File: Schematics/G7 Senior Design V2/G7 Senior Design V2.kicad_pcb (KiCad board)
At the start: 2 copper layers, 100 x 100 mm, 45 parts, among them IC3 UART, J1 USB, J2 JCK, J3 PPTC191LFBN-RC, J4 PPTC191LFBN-RC, Q1 T1, Q2 T2, U1 ESP32-WROOM-32-N4, U2 DWM1000, U3 AMS1117-3.3

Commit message: One Page Error Report Gerber
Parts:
- added G***: LOGO, SD V2 ESP32 Components:UCF Logo 2, F.Cu at (138.5, 102.5)
- added G***: LOGO, SD V2 ESP32 Components:CitronautHeadFootprint, B.Cu at (149.5, 61.0)
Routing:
- net /EN: track 108.0 -> 159.1 mm, vias 6 -> 10
- net Net-(U1-CLK): track 117.6 -> 84.6 mm
- net Net-(Q2-Pad1): track 0.00 -> 28.1 mm, vias 0 -> 2
- net Net-(IC3-DTR): track 7.75 -> 16.6 mm
- net Net-(U1-IO18): track 93.9 -> 89.9 mm
- net /IO0: track 129.1 -> 132.8 mm
- net Net-(IC3-TXD): track 95.2 -> 93.3 mm
- net Net-(U1-IO15): track 44.3 -> 43.1 mm
- net Net-(IC3-VBUS): track 72.4 -> 73.5 mm
- net Net-(U1-CMD): track 91.3 -> 90.4 mm
- net Net-(U1-IO34): track 109.8 -> 109.1 mm
- net GND: track 329.3 -> 328.6 mm
- net Net-(U1-IO2): track 44.0 -> 44.7 mm

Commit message: Updated Gerber and BOM 13 SEP 24
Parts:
- C19: footprint SD V2 USB to UART Components:CAPC2012X95N -> SD V2 USB to UART Components:CAPC2012X145N
- R31: value RD1 -> 1K; footprint SD V2 USB to UART Components:RES_1220_SUS -> SD V2 DW1000 Components:RC0805N_YAG
- R32: value RD2 -> 1K; footprint SD V2 USB to UART Components:RES_1220_SUS -> SD V2 DW1000 Components:RC0805N_YAG
- R33: value RD3 -> 1K; footprint SD V2 USB to UART Components:RES_1220_SUS -> SD V2 DW1000 Components:RC0805N_YAG
- moved R33 0.40 mm to (161.0, 114.6)
- moved R32 0.15 mm to (119.4, 92.5)
- moved C19 0.07 mm to (130.6, 59.0)
- moved R31 0.05 mm to (164.5, 114.6)
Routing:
- net Net-(IC3-VDD): track 168.9 -> 168.2 mm
- net Net-(U2-EXTON): track 30.1 -> 29.4 mm

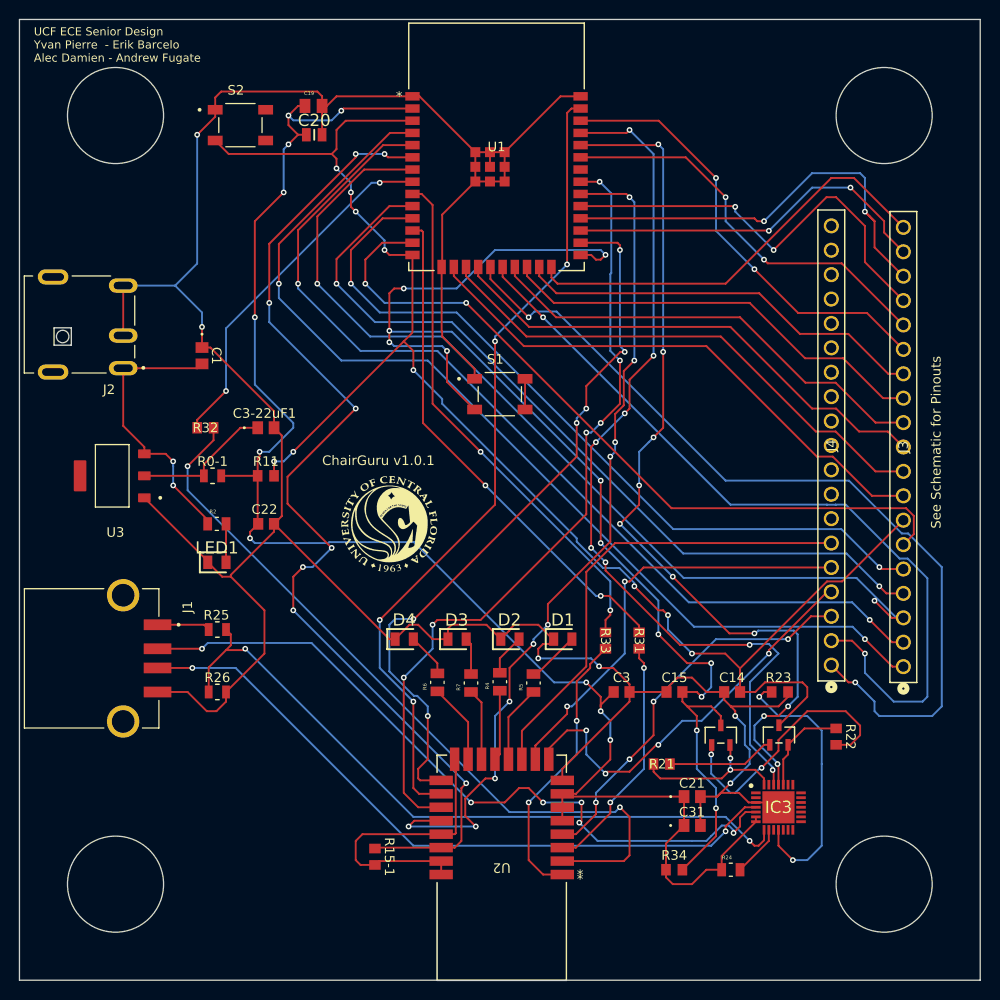
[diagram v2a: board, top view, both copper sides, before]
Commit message: ChairGuru V1.1
Updated Changes According to Doc as of 06 OCT 24.
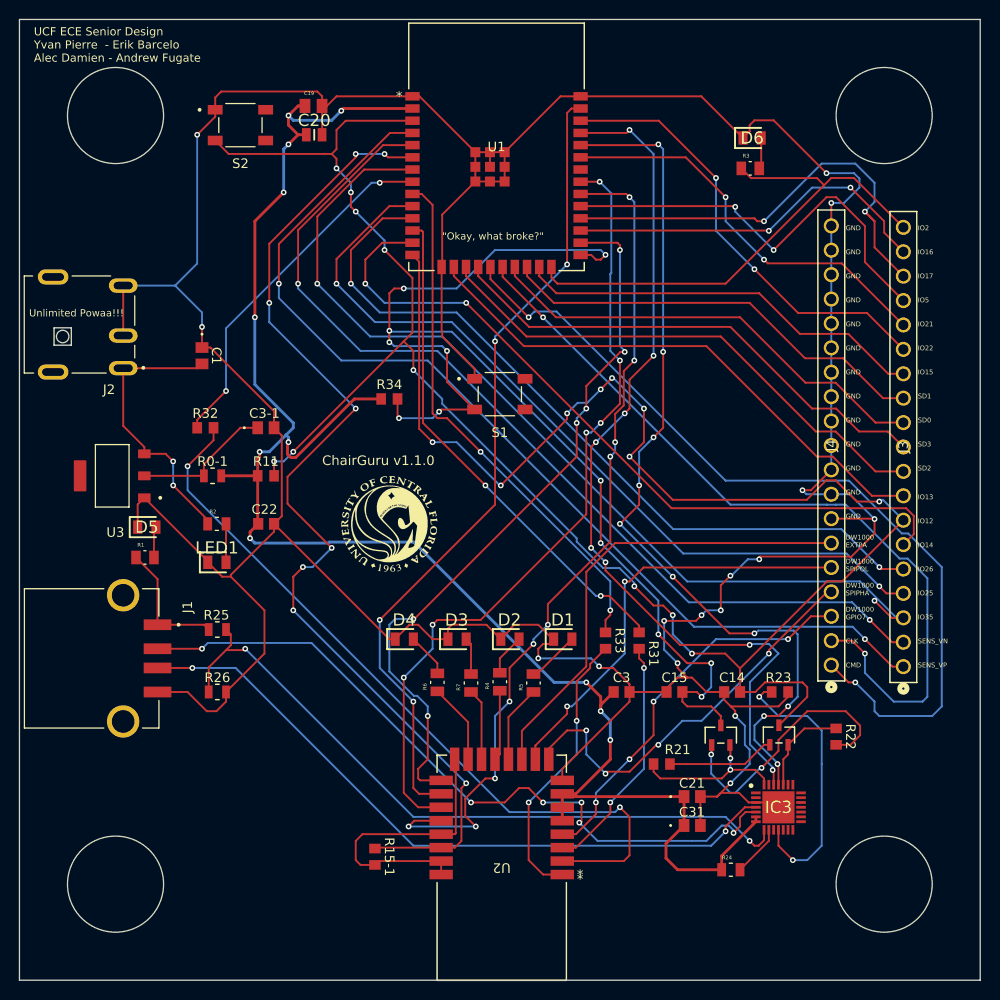
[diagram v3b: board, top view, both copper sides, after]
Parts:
- added D5: LD1, SD V2 DW1000 Components:LEDC2012X90N, F.Cu at (113.3, 102.8)
- added D6: LD1, SD V2 DW1000 Components:LEDC2012X90N, F.Cu at (176.3, 62.3)
- added R1: CRGCQ0805J470R, SD V2 DW1000 Components:RESC2012X65N, F.Cu at (113.1, 106.0)
- added R3: CRGCQ0805J470R, SD V2 DW1000 Components:RESC2012X65N, F.Cu at (176.1, 65.5)
- moved R34 57.3 mm to (138.5, 89.5)
- renumbered C3-22uF1 to C3-1
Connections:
- J3 pad 7: /EN -> Net-(U1-IO12)
- J4 pad 10: unconnected-(J4-Pad10) -> GND
- J4 pad 11: unconnected-(J4-Pad11) -> GND
- J4 pad 12: unconnected-(J4-Pad12) -> GND
- J4 pad 13: unconnected-(J4-Pad13) -> GND
- J4 pad 14: unconnected-(J4-Pad14) -> GND
- J4 pad 15: unconnected-(J4-Pad15) -> GND
- J4 pad 16: unconnected-(J4-Pad16) -> GND
- J4 pad 17: unconnected-(J4-Pad17) -> GND
- J4 pad 18: unconnected-(J4-Pad18) -> GND
- J4 pad 19: unconnected-(J4-Pad19) -> GND
- J4 pad 7: unconnected-(J4-Pad7) -> GND
- J4 pad 8: unconnected-(J4-Pad8) -> GND
- J4 pad 9: unconnected-(J4-Pad9) -> GND
- U1 pad 14: /EN -> Net-(U1-IO12)
- U1 pad 34: Net-(IC3-RXD) -> Net-(IC3-TXD)
- U1 pad 35: Net-(IC3-TXD) -> Net-(IC3-RXD)
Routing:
- net GND: track 329.1 -> 452.4 mm, vias 6 -> 16
- net Net-(U1-IO12): track 0.00 -> 89.3 mm, vias 0 -> 8
- net Net-(IC3-VDD): track 168.2 -> 180.3 mm, vias 10 -> 11
- net /IO0: track 132.8 -> 123.3 mm
- net Net-(U1-IO2): track 44.7 -> 54.0 mm
- net Net-(J1-VCC): track 5.53 -> 13.5 mm
- net Net-(D6-A): track 0.00 -> 3.25 mm
- net Net-(D5-A): track 0.00 -> 3.25 mm
- net (no net): track 3.20 -> 0.00 mm
- net Net-(U1-IO17): track 45.3 -> 47.2 mm
- net /EN: track 159.1 -> 158.0 mm
- net Net-(U1-IO33): track 54.9 -> 55.5 mm
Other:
- board text added: "CLK"
- board text added: "CMD"
- board text added: "ChairGuru v1.1.0"
- board text added: "DW1000 EXTPA"
- board text added: "DW1000 GPIO7"
- board text added: "DW1000 SPIPHA"
- board text added: "DW1000 SPIPOL"
- board text added: "GND"
- board text added: "IO12"
- board text added: "IO13"
- board text added: "IO14"
- board text added: "IO15"
- board text added: "IO16"
- board text added: "IO17"
- board text added: "IO2"
- board text added: "IO21"
- board text added: "IO22"
- board text added: "IO25"
- board text added: "IO26"
- board text added: "IO35"
- board text added: "IO5"
- board text added: "SD0"
- board text added: "SD1"
- board text added: "SD2"
- board text added: "SD3"
- board text added: "SENS_VN"
- board text added: "SENS_VP"
- board text added: "Unlimited Powaa!!!"
- board text added: "{dblquote}Okay, what broke?{dblquote}"
- board text removed: "ChairGuru v1.0.1"
- board text removed: "See Schematic for Pinouts"

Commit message: ChairGuru 7 OCT 24 NIGHT
Andrew's Updated Content
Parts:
- added G***: LOGO, LightningFootprint, F.Cu at (103.0, 81.0)
- added G***: LOGO, SD V2 USB to UART Components:USB File Logo, F.Cu at (107.5, 116.0)
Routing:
- net Net-(IC3-TXD): track 93.3 -> 87.7 mm
- net Net-(IC3-RXD): track 92.8 -> 98.1 mm
- net Net-(U1-IO35): track 98.1 -> 94.3 mm, vias 2 -> 1
- net /IO0: track 123.3 -> 126.0 mm
- net GND: track 452.4 -> 454.6 mm
- net Net-(IC3-SUSPENDB): track 28.8 -> 27.7 mm
- net Net-(D1-A): track 5.50 -> 6.38 mm
- net Net-(U1-IO2): track 54.0 -> 54.7 mm
- net Net-(IC3-VDD): track 180.3 -> 179.8 mm
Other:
- board text added: "ChairGuru v1.2.1"
- board text added: "Unlimited Powaa!"
- board text added: "{dblquote}Ok, what broke?{dblquote}"
- board text removed: "ChairGuru v1.1.0"
- board text removed: "Unlimited Powaa!!!"
- board text removed: "{dblquote}Okay, what broke?{dblquote}"

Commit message: ChairGuru V2.0.1
11 OCT 24 Updates
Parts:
- moved C31 79.4 mm to (116.0, 75.6), turned to -90 degrees
- moved C21 76.7 mm to (134.0, 63.1), turned to -90 degrees
- moved C3 72.0 mm to (118.5, 63.2), turned to -90 degrees
- moved C14 66.7 mm to (131.0, 69.2), turned to 90 degrees
- moved C15 66.0 mm to (126.0, 69.2), turned to -90 degrees
- moved Q1 52.2 mm to (145.5, 84.5)
- moved R24 46.7 mm to (141.5, 105.0), turned to -90 degrees
- moved IC3 45.8 mm to (149.5, 97.0)
- moved R22 44.7 mm to (156.5, 90.1), turned to 90 degrees
- moved R21 44.6 mm to (142.5, 90.1), turned to 90 degrees
- moved Q2 44.5 mm to (153.5, 84.5)
- moved C22 34.9 mm to (136.0, 69.2), turned to -90 degrees
- moved G*** 33.8 mm to (125.0, 133.5)
- moved R11 29.9 mm to (116.0, 69.1), turned to -90 degrees
- moved R34 26.8 mm to (121.0, 69.1), turned to -90 degrees
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- renumbered S2 to EN, S1 to IO0
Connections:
- J4 pad 11: GND -> Net-(U2-GPIO6/EXTRXE/SPIPHA)
- J4 pad 14: GND -> Net-(U2-GPIO5/EXTTXE/SPIPOL)
- J4 pad 17: GND -> Net-(U2-GPIO4/EXTPA)
- J4 pad 2: Net-(U1-CLK) -> GND
- J4 pad 3: Net-(U2-GPIO7) -> GND
- J4 pad 4: Net-(U2-GPIO6/EXTRXE/SPIPHA) -> GND
- J4 pad 5: Net-(U2-GPIO5/EXTTXE/SPIPOL) -> Net-(U1-CLK)
- J4 pad 6: Net-(U2-GPIO4/EXTPA) -> GND
- J4 pad 8: GND -> Net-(U2-GPIO7)
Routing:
- net Net-(U1-IO23): track 84.5 -> 174.8 mm
- net /EN: track 158.0 -> 73.7 mm, vias 10 -> 4
- net Net-(U1-IO25): track 85.1 -> 160.4 mm, vias 2 -> 7
- net Net-(IC3-RXD): track 98.1 -> 43.1 mm, vias 10 -> 4
- net /IO0: track 126.0 -> 72.0 mm, vias 12 -> 4
- net Net-(U1-IO33): track 55.5 -> 108.8 mm, vias 2 -> 4
- net Net-(U1-IO26): track 81.1 -> 130.6 mm, vias 2 -> 7
- net Net-(IC3-TXD): track 87.7 -> 43.7 mm, vias 8 -> 6
- net Net-(U1-IO12): track 89.1 -> 132.6 mm, vias 8 -> 12
- net Net-(U2-GPIO4/EXTPA): track 49.0 -> 89.9 mm, vias 0 -> 4
- net Net-(IC3-D-): track 76.5 -> 40.6 mm, vias 6 -> 2
- net Net-(U1-IO35): track 94.3 -> 130.1 mm, vias 1 -> 7
- net Net-(IC3-VBUS): track 73.5 -> 38.7 mm, vias 2 -> 0
- net Net-(U2-GPIO5/EXTTXE/SPIPOL): track 44.8 -> 78.1 mm
- net Net-(IC3-D+): track 71.9 -> 41.3 mm
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- added copper zone on B.Cu, net GND
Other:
- board text added: "ChairGuru v2.0.1"
- board text added: "{dblquote}Okay, what broke?{dblquote}"
- board text removed: "ChairGuru v1.2.1"
- board text removed: "{dblquote}Ok, what broke?{dblquote}"
